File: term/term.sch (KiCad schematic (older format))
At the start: 13 parts, among them P101 CONN_01X08, P102 XG4C-1631, P103 CONN_01X08, SW101 SW_PUSH

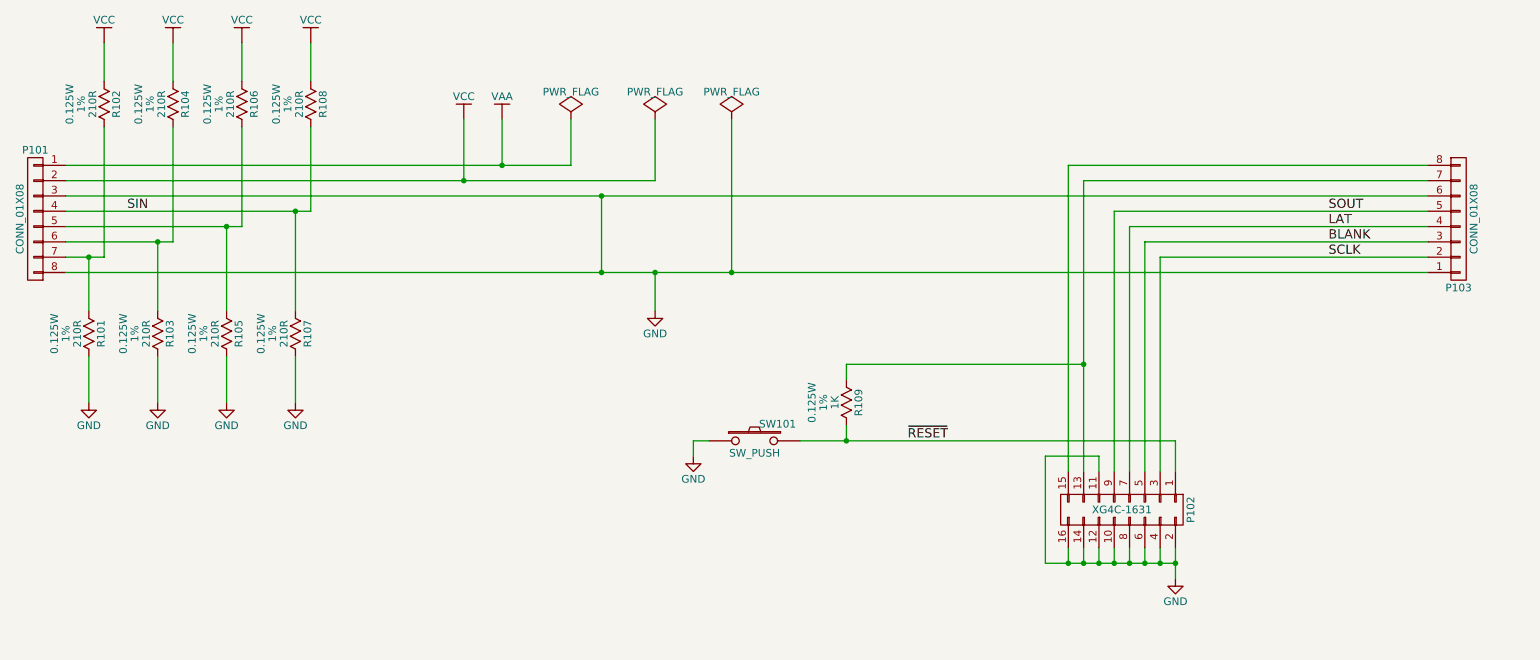
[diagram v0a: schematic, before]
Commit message: Add wire pads for display power. Generate gerbers for termination board. Upload to OSHPark.
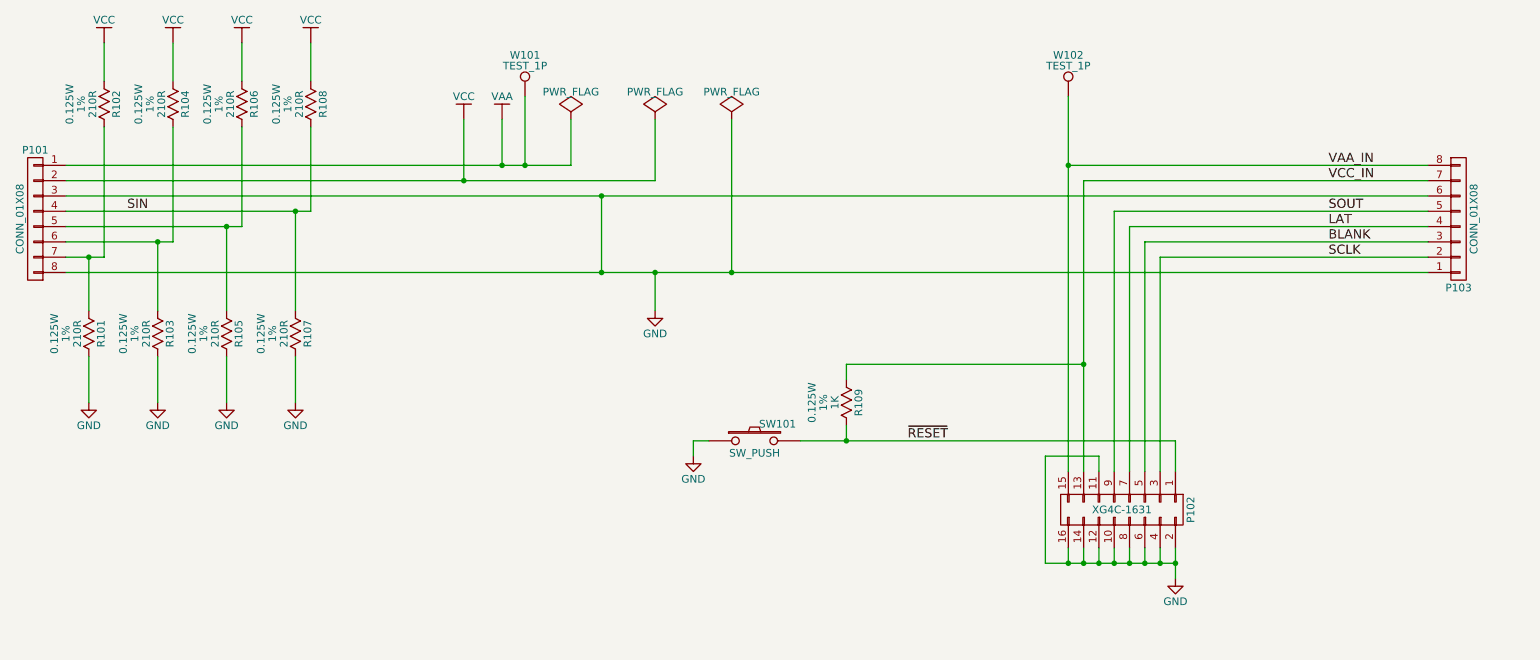
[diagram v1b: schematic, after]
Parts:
- added W101, W102: TEST_1P, Wire_Pads:SolderWirePad_single_1mmDrill, symbol TEST_1P
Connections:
- net VAA: now also W101.1
- net VCC_IN: now reaches P102.13 (P13), P103.7 (P7), R109.1
- net VAA_IN: now reaches P102.15 (P15), P103.8 (P8)
- net VAA_IN: now also W102.1
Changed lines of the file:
@@
 Connection ~ 7900 5300
 Wire Wire Line
-	7900 2700 7900 4700
+	7900 2250 7900 4700
 Wire Wire Line
 	8000 2800 8000 4700
@@
 	6450 4000 8000 4000
 Connection ~ 8000 4000
+Text Label 9600 2700 0    60   ~ 0
+VAA_IN
+Text Label 9600 2800 0    60   ~ 0
+VCC_IN
+$Comp
+L TEST_1P W101
+U 1 1 57649C24
+P 4350 2250
+F 0 "W101" H 4350 2520 50  0000 C CNN
+F 1 "TEST_1P" H 4350 2450 50  0000 C CNN
+F 2 "Wire_Pads:SolderWirePad_single_1mmDrill" H 4550 2250 50  0001 C CNN
+F 3 "" H 4550 2250 50  0000 C CNN
+	1    4350 2250
+	1    0    0    -1
+$EndComp
+Wire Wire Line
+	4350 2250 4350 2700
+Connection ~ 4350 2700
+$Comp
+L TEST_1P W102
+U 1 1 57649E09
+P 7900 2250
+F 0 "W102" H 7900 2520 50  0000 C CNN
+F 1 "TEST_1P" H 7900 2450 50  0000 C CNN
+F 2 "Wire_Pads:SolderWirePad_single_1mmDrill" H 8100 2250 50  0001 C CNN
+F 3 "" H 8100 2250 50  0000 C CNN
+	1    7900 2250
+	1    0    0    -1
+$EndComp
+Connection ~ 7900 2700
 $EndSCHEMATC

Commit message: New version of the termination/connector board. Add LED indicators for status and power.
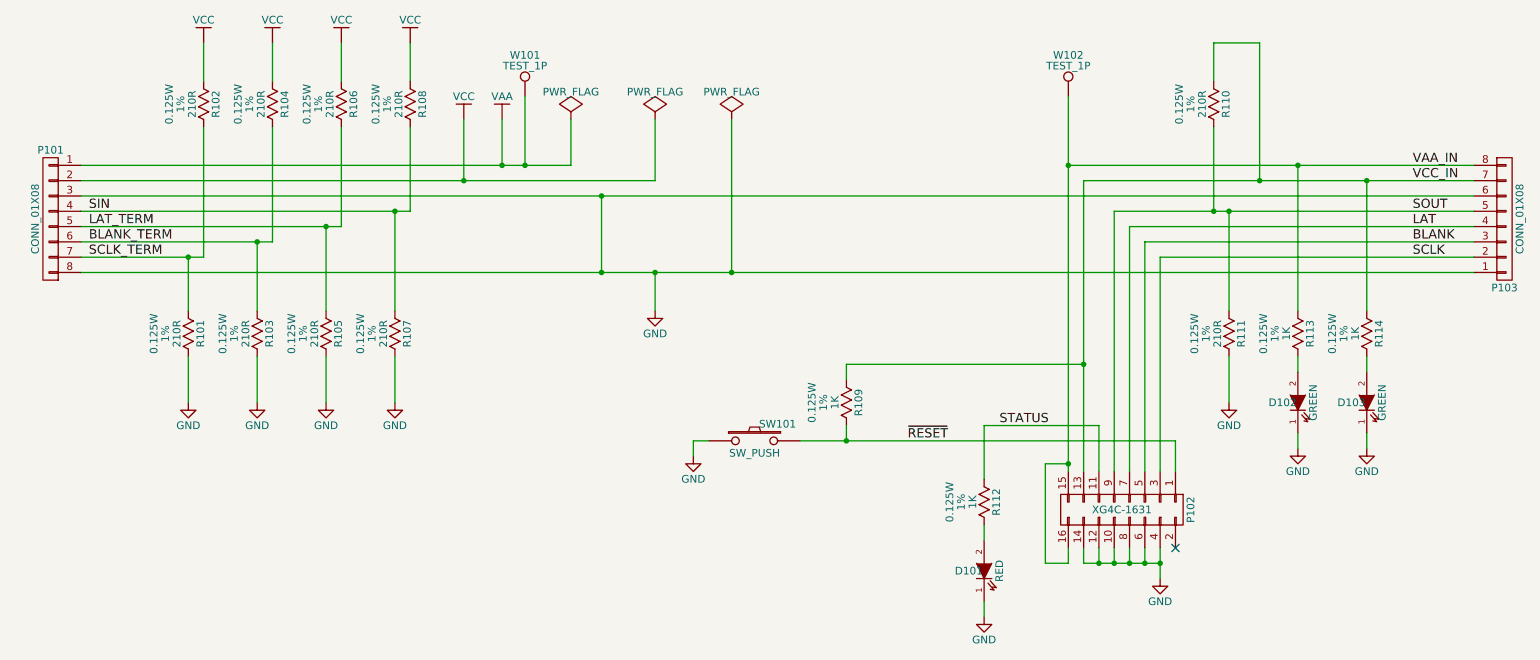
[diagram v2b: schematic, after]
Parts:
- added D101: RED, local:LED_0805_HandSoldering, symbol LED
- added D102, D103: GREEN, local:LED_0805_HandSoldering, symbol LED
- added R110, R111: 210R, local:R_0805_HandSoldering, symbol R_local
- added R112, R113, R114: 1K, local:R_0805_HandSoldering, symbol R_local
- R101, R102, R103, R104, R105, R106, R107, R108, R109: footprint Resistors_SMD:R_0805_HandSoldering -> local:R_0805_HandSoldering
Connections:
- net GND: now also D101.1 (K), D102.1 (K), D103.1 (K), R111.2; no longer P102.11 (P11), P102.16 (P16), P102.2 (P2)
- net SOUT: now also R110.2, R111.1
- net VAA_IN: now also P102.16 (P16), R113.1
- net VCC_IN: now also R110.1, R114.1
- net LAT_TERM: now reaches P101.5 (P5), R105.1, R106.2
- net BLANK_TERM: now reaches P101.6 (P6), R103.1, R104.2
- net SCLK_TERM: now reaches P101.7 (P7), R101.1, R102.2
- new net: D101.2 (A), R112.2
- new net: D103.2 (A), R114.2
- new net: D102.2 (A), R113.2
- new net STATUS: P102.11 (P11), R112.1
- no-connect marks 0 -> 1
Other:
- moved on the sheet: P101, P103, R101, R102, R103, R104, R105, R106, R107, R108

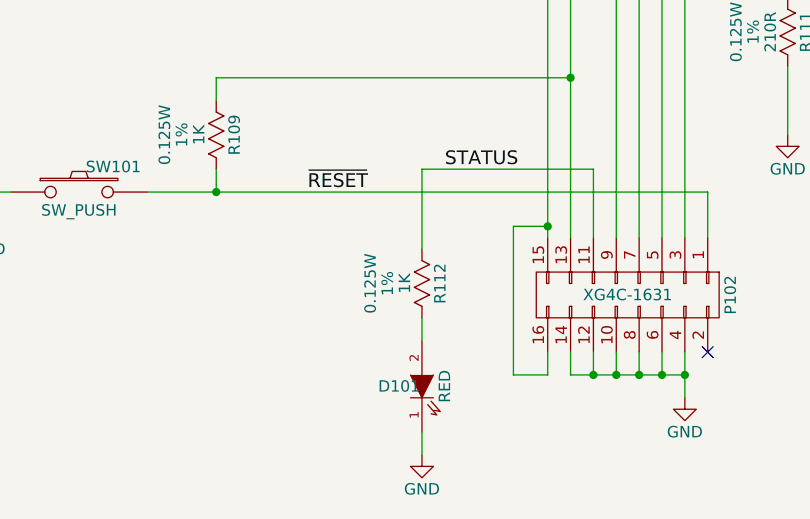
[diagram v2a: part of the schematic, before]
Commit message: Add power indication LEDs.
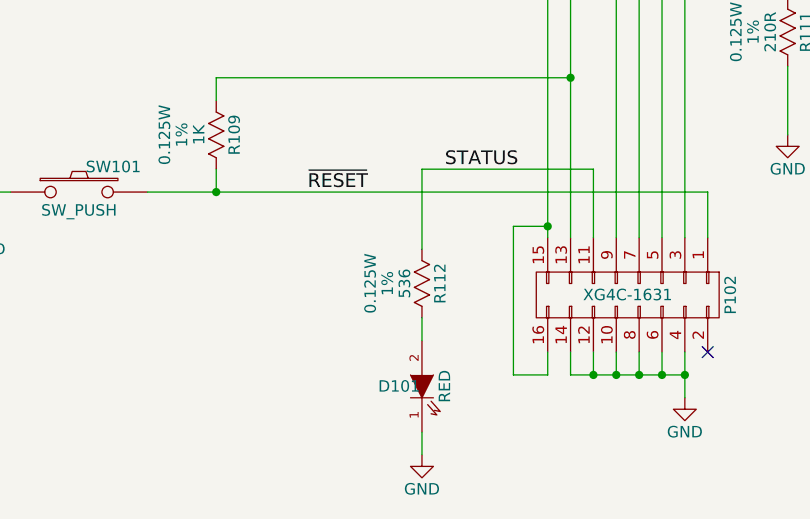
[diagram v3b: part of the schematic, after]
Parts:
- R112: value 1K -> 536; PartNum CRCW08051K00FKEA -> CRCW0805536RFKEA
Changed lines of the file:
@@
 P 7350 4900
 F 0 "R112" V 7430 4900 50  0000 C CNN
-F 1 "1K" V 7275 4900 50  0000 C CNN
+F 1 "536" V 7275 4900 50  0000 C CNN
 F 2 "local:R_0805_HandSoldering" V 7280 4900 30  0001 C CNN
 F 3 "" V 7430 4900 30  0000 C CNN
@@
 F 5 "0.125W" V 7125 4900 50  0000 C CNN "Power"
 F 6 "Vishay Dale" V 7350 4900 50  0001 C CNN "Manufacturer"
-F 7 "CRCW08051K00FKEA" V 7500 4900 50  0001 C CNN "PartNum"
+F 7 "CRCW0805536RFKEA" V 7500 4900 50  0001 C CNN "PartNum"
 	1    7350 4900
 	1    0    0    -1

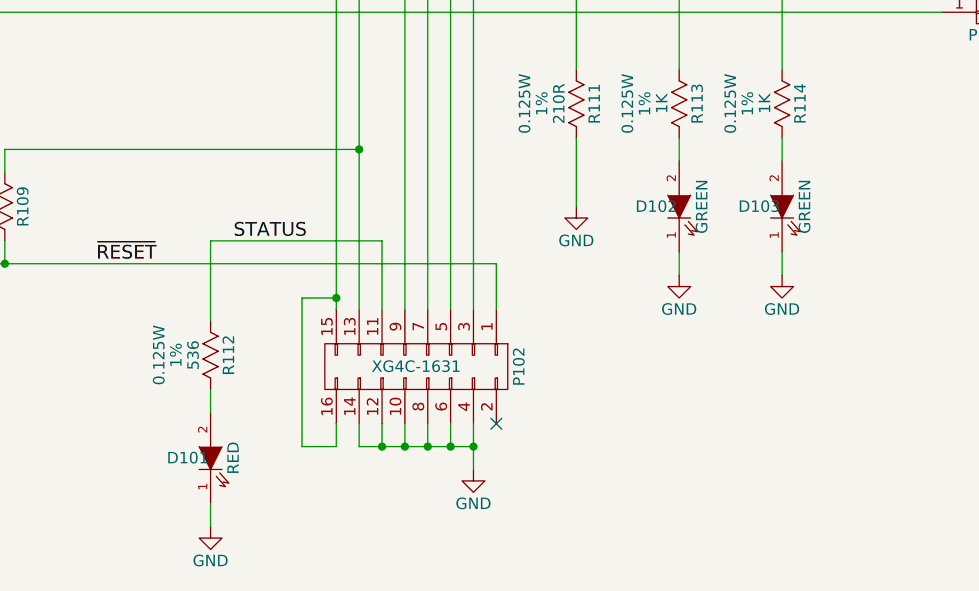
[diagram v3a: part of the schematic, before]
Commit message: Termination board:   Use power symbols from local library.   Generate gerbers.   Generate pdf schematic.   Generate BOM.
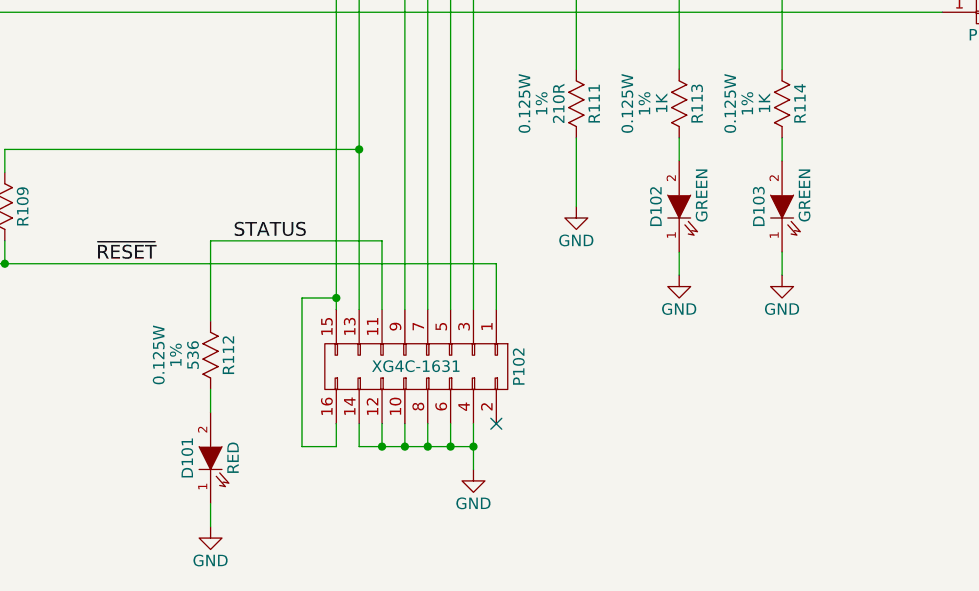
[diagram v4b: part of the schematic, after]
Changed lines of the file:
@@
 EESchema Schematic File Version 2
+LIBS:local
 LIBS:power
 LIBS:device
@@
 LIBS:contrib
 LIBS:valves
-LIBS:local
 LIBS:term-cache
 EELAYER 25 0
@@
 U 1 1 588FEDC4
 P 7350 5350
-F 0 "D101" V 7350 5450 50  0000 C CNN
+F 0 "D101" H 7350 5450 50  0000 C CNN
 F 1 "RED" H 7350 5250 50  0000 C CNN
 F 2 "local:LED_0805_HandSoldering" H 7350 5350 50  0001 C CNN
@@
 U 1 1 58900877
 P 9850 4250
-F 0 "D103" V 9850 4350 50  0000 C CNN
-F 1 "GREEN" H 9850 4150 50  0000 C CNN
+F 0 "D103" H 9850 4350 50  0000 C CNN
+F 1 "GREEN" H 9900 4150 50  0000 C CNN
 F 2 "local:LED_0805_HandSoldering" H 9850 4250 50  0001 C CNN
 F 3 "" H 9850 4250 50  0000 C CNN
@@
 U 1 1 58900B79
 P 9400 4250
-F 0 "D102" V 9400 4350 50  0000 C CNN
-F 1 "GREEN" H 9400 4150 50  0000 C CNN
+F 0 "D102" H 9400 4350 50  0000 C CNN
+F 1 "GREEN" H 9450 4150 50  0000 C CNN
 F 2 "local:LED_0805_HandSoldering" H 9400 4250 50  0001 C CNN
 F 3 "" H 9400 4250 50  0000 C CNN

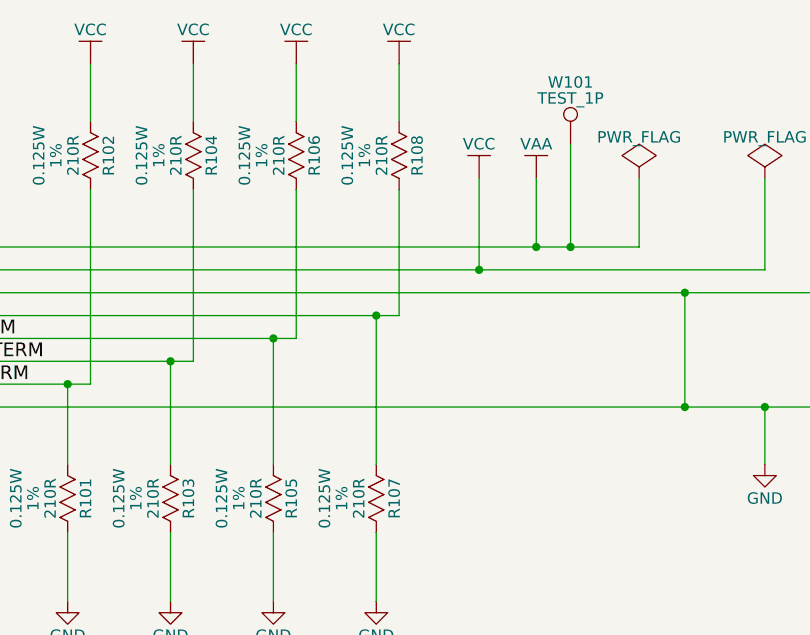
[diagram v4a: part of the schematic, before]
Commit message: Add DNP to unused resistors on the termination board. Minor clean up of clock board.
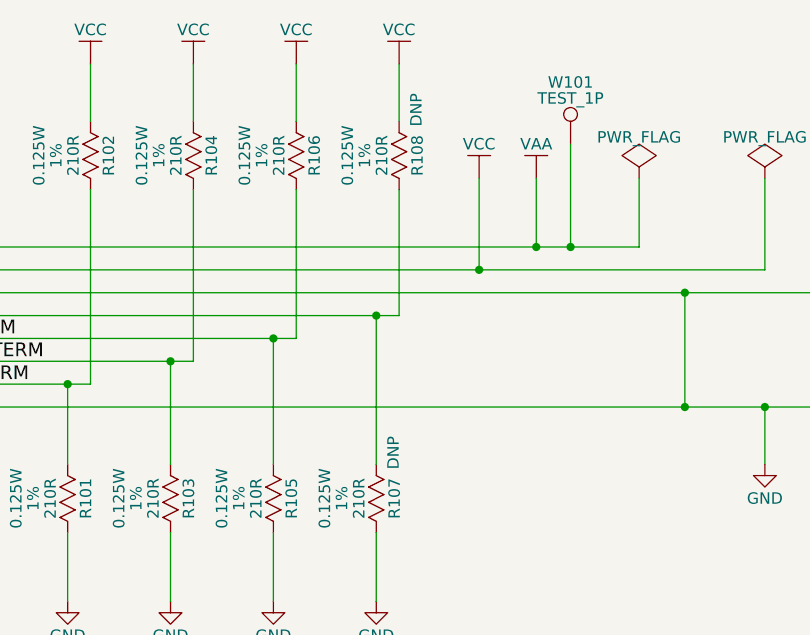
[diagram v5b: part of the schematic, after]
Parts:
- R107, R108: DNP (none) -> DNP
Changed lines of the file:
@@
 F 6 "Vishay Dale" V 3500 3800 50  0001 C CNN "Manufacturer"
 F 7 "CRCW0805210RFKEA" V 3650 3800 50  0001 C CNN "PartNum"
+F 8 "DNP" V 3575 4000 50  0000 C CNN "DNP"
 	1    3500 3800
 	1    0    0    -1
@@
 F 6 "Vishay Dale" V 3600 2300 50  0001 C CNN "Manufacturer"
 F 7 "CRCW0805210RFKEA" V 3750 2300 50  0001 C CNN "PartNum"
+F 8 "DNP" V 3675 2500 50  0000 C CNN "DNP"
 	1    3600 2300
 	1    0    0    -1

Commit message: Update term board to kicad 5.1. Regenerate output files.
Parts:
- D101, D102, D103: symbol LED -> Local:LED
- P101, P103: symbol CONN_01X08 -> conn:CONN_01X08
- P102: symbol CONN_02X08 -> conn:CONN_02X08
- R101, R102, R103, R104, R105, R106, R107, R108, R109, R110, R111, R112, R113, R114: symbol R_local -> Local:R_local
- SW101: symbol SW_PUSH -> Switch:SW_Push
- W101, W102: symbol TEST_1P -> conn:TEST_1P

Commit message: Fix terminator board to point to 5.1 symbol libraries.
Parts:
- P101, P103: symbol conn:CONN_01X08 -> Connector_Generic:Conn_01x08
- P102: symbol conn:CONN_02X08 -> Connector_Generic:Conn_02x08_Odd_Even
- W101, W102: value TEST_1P -> TestPoint; symbol conn:TEST_1P -> Connector:TestPoint
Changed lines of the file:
@@
 $EndDescr
 $Comp
-L conn:CONN_01X08 P101
+L Connector_Generic:Conn_01x08 P101
 U 1 1 5597595F
-P 1250 3050
-F 0 "P101" H 1250 3500 50  0000 C CNN
-F 1 "CONN_01X08" V 1350 3050 50  0000 C CNN
-F 2 "local:Pin_Header_1x08_square" H 1250 3050 60  0001 C CNN
-F 3 "" H 1250 3050 60  0000 C CNN
-	1    1250 3050
+P 1250 3000
+F 0 "P101" H 1250 3450 50  0000 C CNN
+F 1 "CONN_01X08" V 1350 3000 50  0000 C CNN
+F 2 "local:Pin_Header_1x08_square" H 1250 3000 60  0001 C CNN
+F 3 "" H 1250 3000 60  0000 C CNN
+	1    1250 3000
 	-1   0    0    -1
 $EndComp
 $Comp
-L conn:CONN_01X08 P103
+L Connector_Generic:Conn_01x08 P103
 U 1 1 559759A0
-P 10750 3050
-F 0 "P103" H 10750 3500 50  0000 C CNN
-F 1 "CONN_01X08" V 10850 3050 50  0000 C CNN
-F 2 "local:Pin_Header_1x08_square" H 10750 3050 60  0001 C CNN
-F 3 "" H 10750 3050 60  0000 C CNN
-	1    10750 3050
+P 10750 3100
+F 0 "P103" H 10750 3550 50  0000 C CNN
+F 1 "CONN_01X08" V 10850 3100 50  0000 C CNN
+F 2 "local:Pin_Header_1x08_square" H 10750 3100 60  0001 C CNN
+F 3 "" H 10750 3100 60  0000 C CNN
+	1    10750 3100
 	1    0    0    1
 $EndComp
@@
 $EndComp
 $Comp
-L conn:CONN_02X08 P102
+L Connector_Generic:Conn_02x08_Odd_Even P102
 U 1 1 57543F5D
-P 8250 4950
-F 0 "P102" H 8250 5400 50  0000 C CNN
-F 1 "XG4C-1631" V 8250 4950 50  0000 C CNN
-F 2 "local:XG4C-1631" H 8250 3750 50  0001 C CNN
-F 3 "" H 8250 3750 50  0000 C CNN
-F 4 "Omron Electronics" H 8250 4950 60  0001 C CNN "Manufacturer"
-F 5 "XG4C-1631" H 8250 4950 60  0001 C CNN "PartNum"
-	1    8250 4950
+P 8300 4900
+F 0 "P102" H 8350 5300 50  0000 C CNN
+F 1 "XG4C-1631" V 8350 4800 50  0000 C CNN
+F 2 "local:XG4C-1631" H 8300 3700 50  0001 C CNN
+F 3 "" H 8300 3700 50  0000 C CNN
+F 4 "Omron Electronics" H 8300 4900 60  0001 C CNN "Manufacturer"
+F 5 "XG4C-1631" H 8300 4900 60  0001 C CNN "PartNum"
+	1    8300 4900
 	0    1    1    0
 $EndComp
@@
 VCC_IN
 $Comp
-L conn:TEST_1P W101
+L Connector:TestPoint W101
 U 1 1 57649C24
 P 4350 2250
 F 0 "W101" H 4350 2520 50  0000 C CNN
-F 1 "TEST_1P" H 4350 2450 50  0000 C CNN
+F 1 "TestPoint" H 4350 2450 50  0000 C CNN
 F 2 "Wire_Pads:SolderWirePad_single_1mmDrill" H 4550 2250 50  0001 C CNN
 F 3 "" H 4550 2250 50  0000 C CNN
@@
 $EndComp
 $Comp
-L conn:TEST_1P W102
+L Connector:TestPoint W102
 U 1 1 57649E09
 P 7900 2250
 F 0 "W102" H 7900 2520 50  0000 C CNN
-F 1 "TEST_1P" H 7900 2450 50  0000 C CNN
+F 1 "TestPoint" H 7900 2450 50  0000 C CNN
 F 2 "Wire_Pads:SolderWirePad_single_1mmDrill" H 8100 2250 50  0001 C CNN
 F 3 "" H 8100 2250 50  0000 C CNN
